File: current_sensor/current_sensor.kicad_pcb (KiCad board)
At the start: 2 copper layers, 26 parts, among them Q1 S8050, Q2 S8550, U1 TL431LP, U2 TL062, U3 LM393, U4 TL062

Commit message: Finished PCB Design
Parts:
- C1, C2, C3: footprint Capacitor_THT:C_Disc_D5.0mm_W2.5mm_P2.50mm -> Capacitor_THT:C_Disc_D5.0mm_W2.5mm_P5.00mm
- moved Power_input_output1 80.9 mm to (61.7, 76.8), turned to -90 degrees
- moved C1 68.5 mm to (94.7, 101.5), turned to 180 degrees
- moved R_Shunt2 67.9 mm to (70.7, 75.9), turned to -90 degrees
- moved RV3 59.5 mm to (100.6, 97.0)
- moved RV2 58.2 mm to (100.6, 88.3)
- moved R_Shunt1 53.4 mm to (81.8, 75.9), turned to -90 degrees
- moved U1 53.2 mm to (108.8, 97.3), turned to 90 degrees
- moved RV1 48.3 mm to (104.3, 94.0)
- moved C2 47.9 mm to (117.0, 101.1)
- moved U2 44.9 mm to (88.5, 90.7)
- moved R6 39.7 mm to (88.4, 75.7)
- moved R3 33.1 mm to (88.4, 78.7)
- moved Q2 32.7 mm to (129.9, 89.8), turned to -90 degrees
- moved Q1 32.5 mm to (130.5, 101.1), turned to 90 degrees
- moved C3 31.5 mm to (138.9, 99.7)
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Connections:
- RV1 pad 3: unconnected-(RV1-Pad3) -> Net-(U1-REF)
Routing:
- net GND: track 0.00 -> 142.0 mm
- net +12V: track 0.00 -> 140.5 mm
- net V_current_divided: track 0.00 -> 79.8 mm
- net VS: track 0.00 -> 57.6 mm
- net V_current: track 0.00 -> 53.0 mm
- net Net-(U2A--): track 0.00 -> 40.4 mm
- net Net-(Q2-C): track 0.00 -> 31.2 mm
- net Net-(Q1-B): track 0.00 -> 30.7 mm
- net Net-(U2A-+): track 0.00 -> 27.1 mm
- net uC Protection REFRENCE: track 0.00 -> 25.2 mm
- net Net-(Q2-B): track 0.00 -> 18.1 mm
- net V_current_divided_clamped: track 0.00 -> 16.5 mm
- net Net-(U1-REF): track 0.00 -> 11.3 mm
- net Net-(U3A-+): track 0.00 -> 9.62 mm
- net Net-(Q1-C): track 0.00 -> 5.10 mm
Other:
- board outline added: 89.9 x 31.6 mm

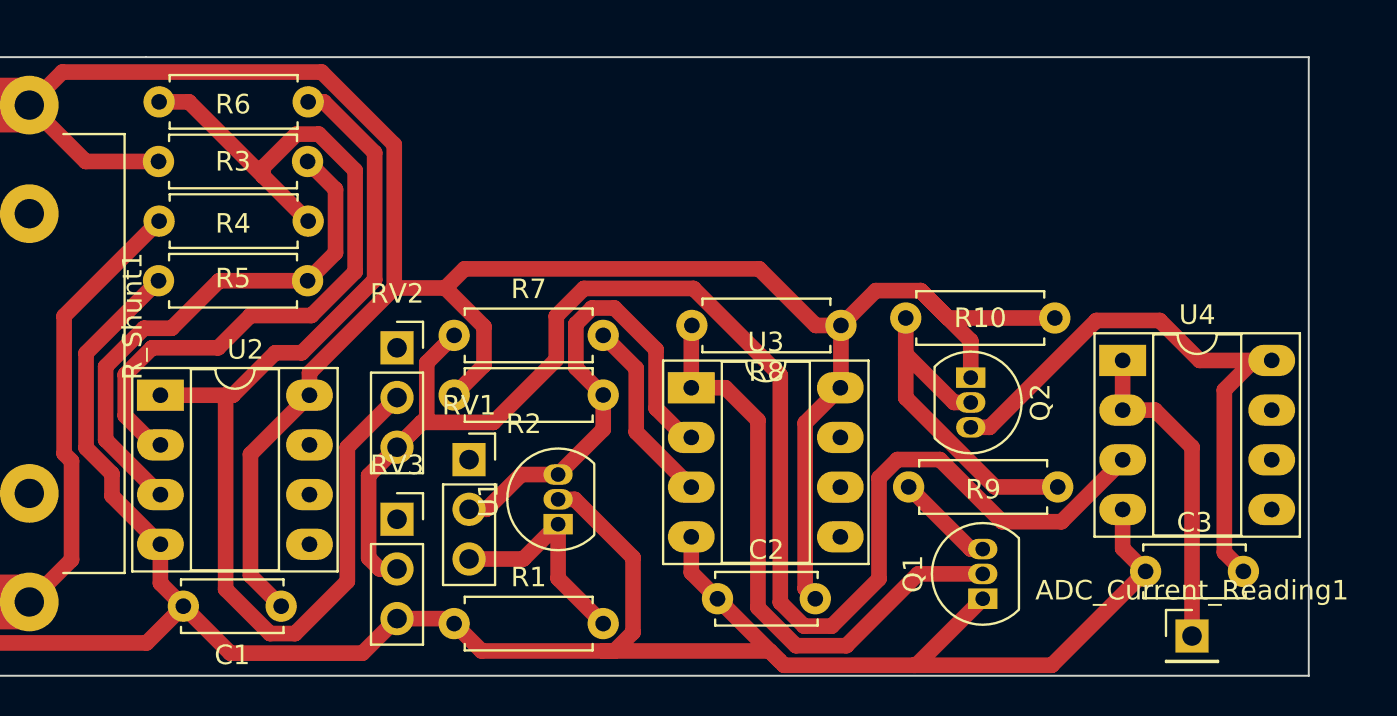
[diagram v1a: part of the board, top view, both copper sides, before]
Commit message: minor modifications to help PCB CAM
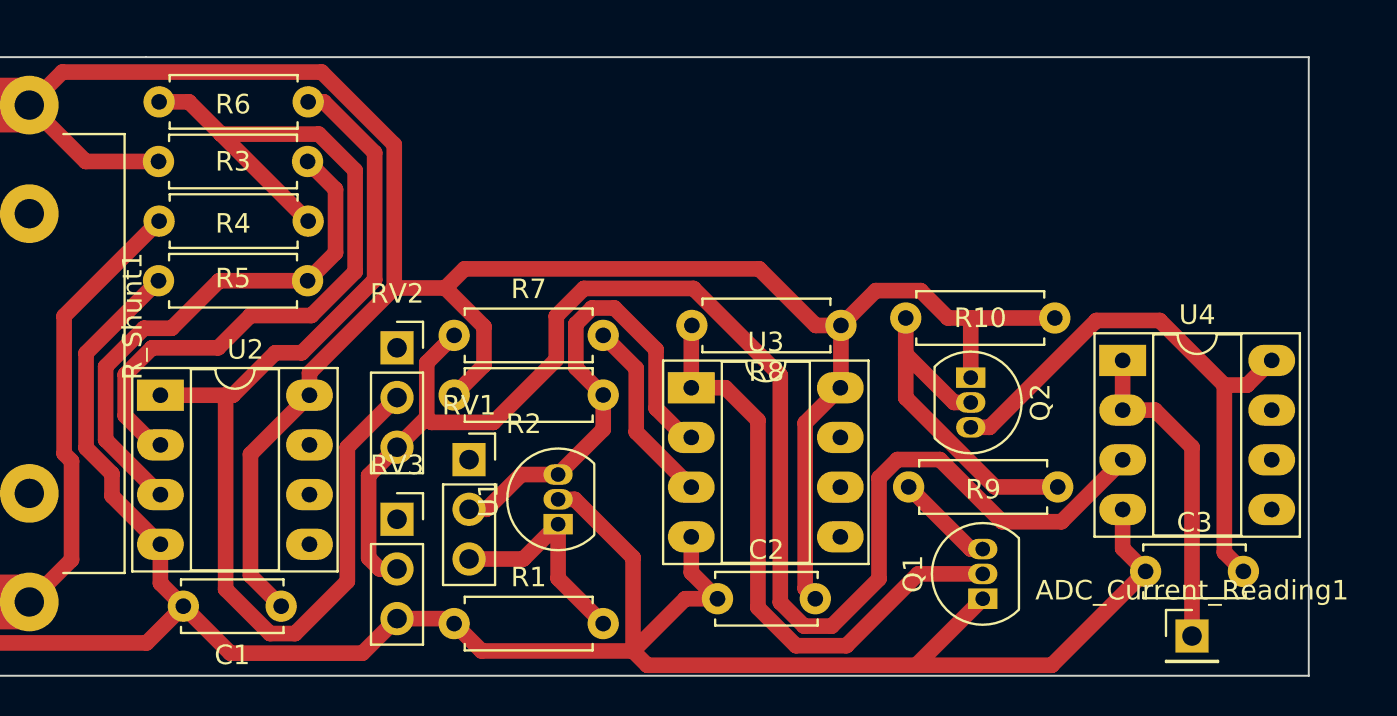
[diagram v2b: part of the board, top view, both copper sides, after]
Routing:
- net +12V: track 140.5 -> 138.1 mm
- net V_current_divided: track 79.8 -> 77.8 mm
- net Net-(Q2-C): track 31.2 -> 29.5 mm
- net Net-(U2A--): track 40.4 -> 41.4 mm

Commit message: Final Version Ready
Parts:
- removed ADC_Current_Reading1: Conn_01x01_Socket, Connector_PinHeader_2.54mm:PinHeader_1x01_P2.54mm_Vertical
- added J1: Conn_01x02_Socket, Connector_PinSocket_2.54mm:PinSocket_1x02_P2.54mm_Vertical, F.Cu at (142.7, 103.1)
- moved R1 0.18 mm to (103.6, 102.5)
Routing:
- net GND: track 141.9 -> 146.5 mm
- net VS: track 57.6 -> 56.7 mm
- net V_current_divided_clamped: track 16.5 -> 17.3 mm
